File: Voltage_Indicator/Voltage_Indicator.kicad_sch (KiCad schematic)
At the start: 20 parts, among them IC1 TLV2371QDBVRQ1, J1 PET-02-XX-X-VT-LC, U2 IPBT-102-H1-XX-S-RA, U3 PAMC0381D10QDFXRQ1

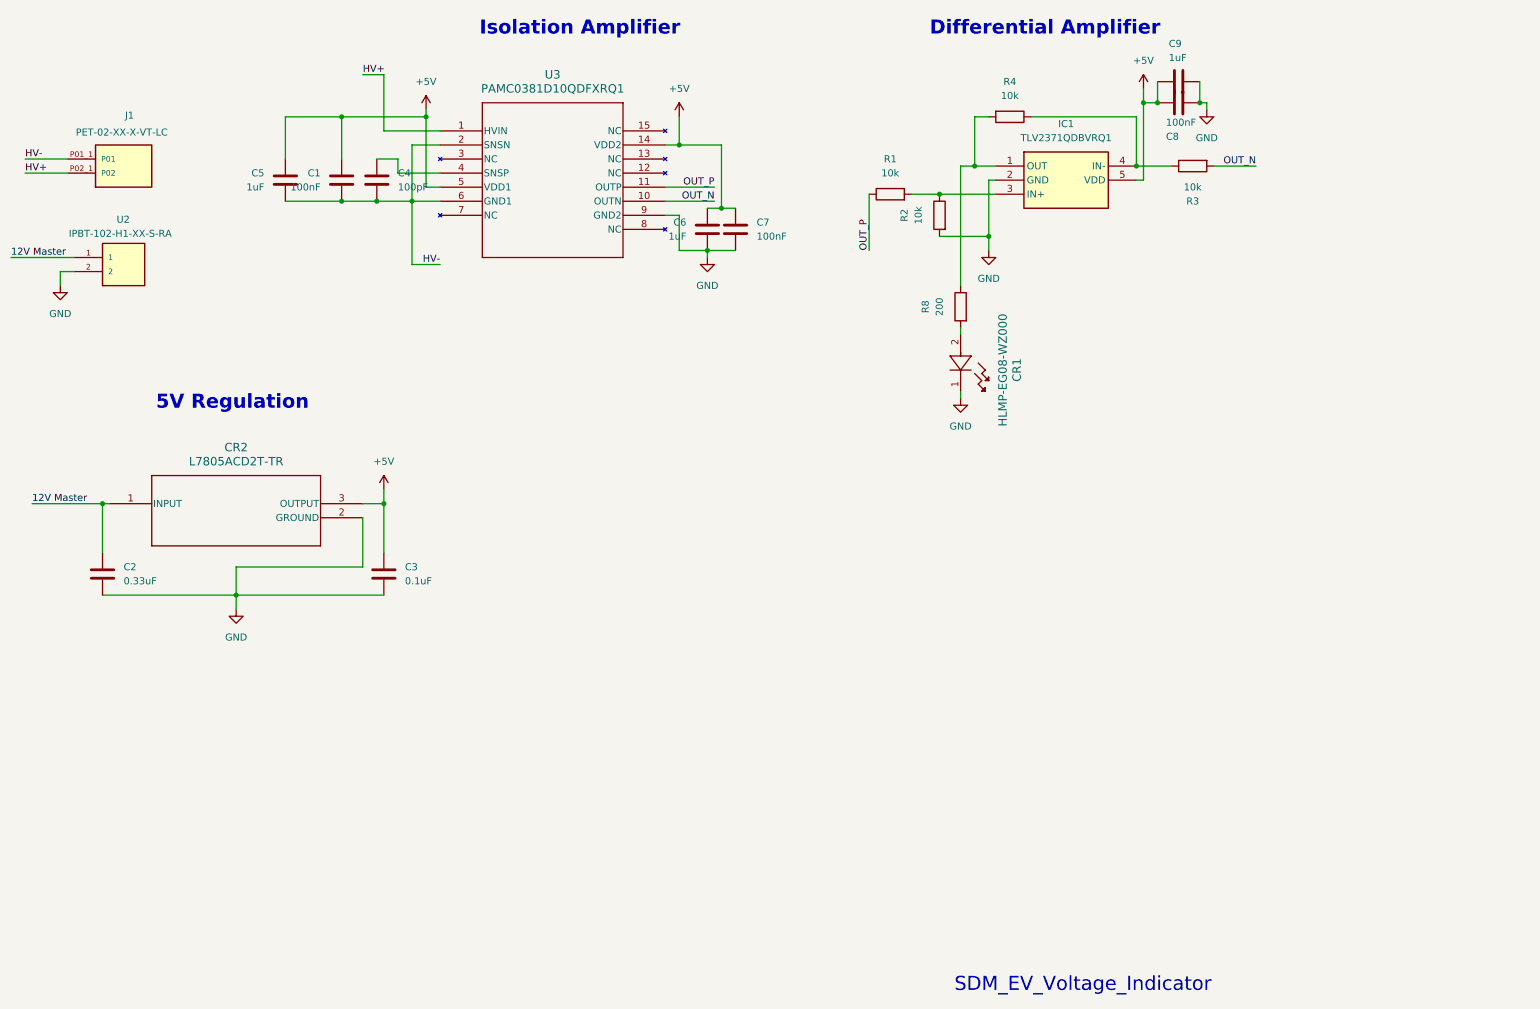
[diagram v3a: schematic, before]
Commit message: Voltage Indicator with comparator :(
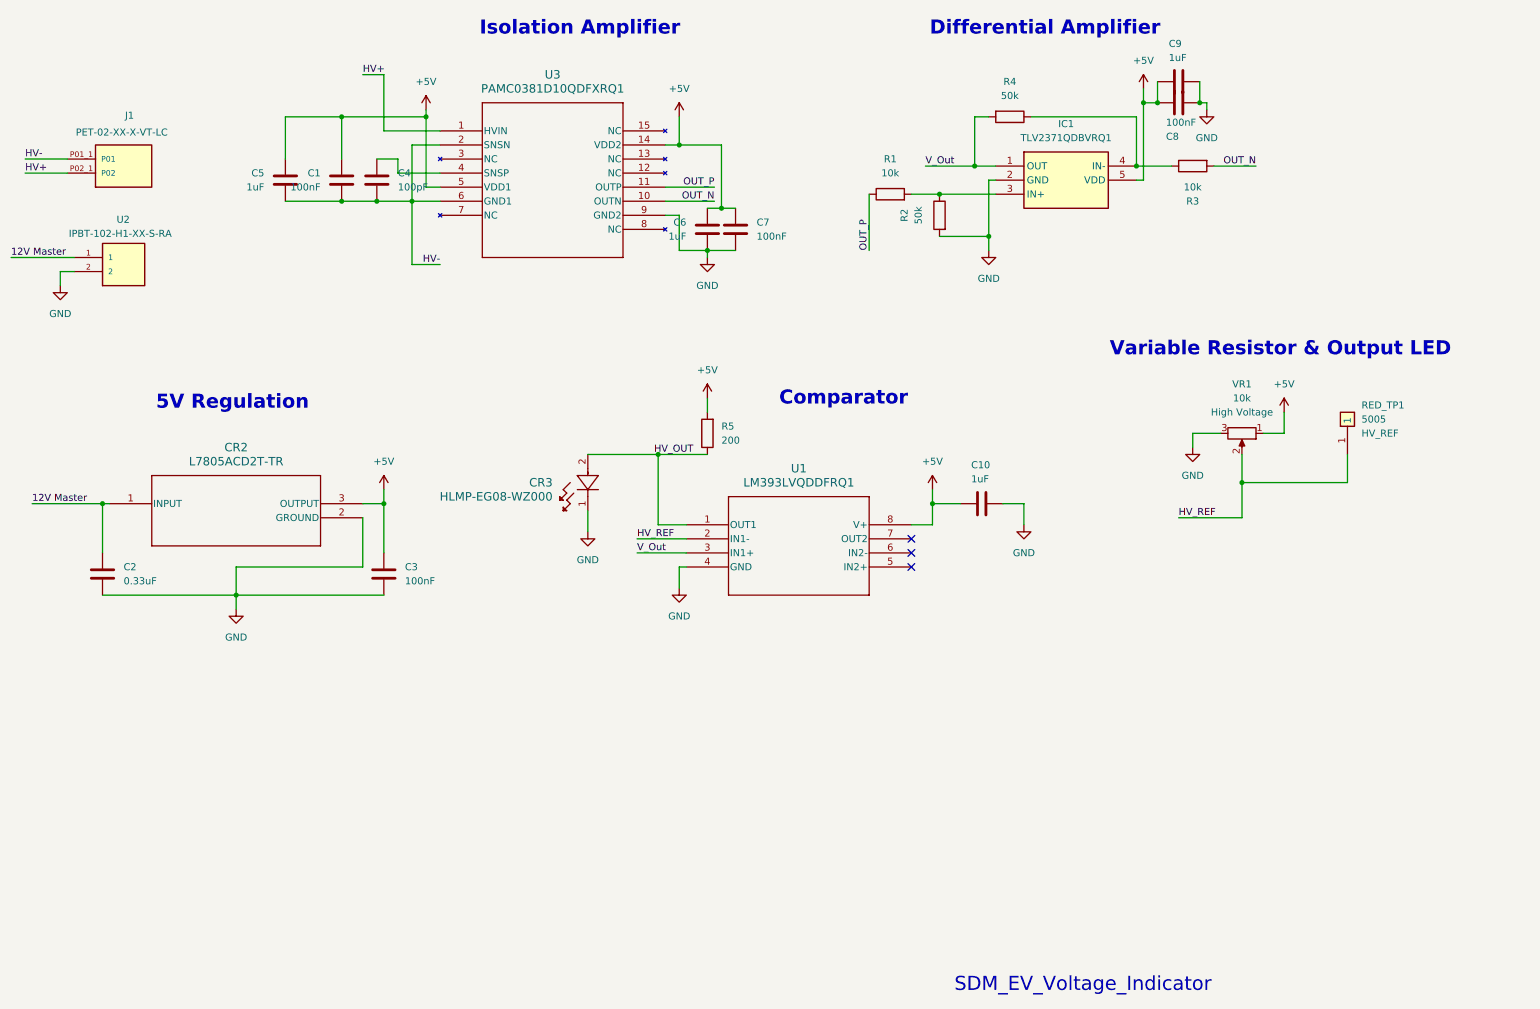
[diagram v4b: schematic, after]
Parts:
- removed CR1: HLMP-EG08-WZ000, Footprints:LED_AVAGO_HLMP_XX08_AVA, symbol Symbols:HLMP-EG08-WZ000
- removed R8: 200, Resistor_SMD:R_0201_0603Metric, symbol Device:R
- added C10: 1uF, Capacitor_SMD:C_0603_1608Metric, symbol Device:C
- added CR3: HLMP-EG08-WZ000, Footprints:LED_AVAGO_HLMP_XX08_AVA, symbol Symbols:HLMP-EG08-WZ000
- added R5: 200, Resistor_SMD:R_0603_1608Metric, symbol Device:R
- added RED_TP1: 5005, SDM_MiscFootprint:5005, symbol SDM_TESTPOINT:5005
- added U1: LM393LVQDDFRQ1, Footprints:SOT-23-THIN8_DDF_TEX, symbol SDM_Parts:LM393LVQDDFRQ1
- added VR1: 10k, SDM_MiscFootprint:3386P1103TLF, symbol SDM_VARIABLE_RESISTOR:3386P-1-103TLF
- C3: value 0.1uF -> 100nF
- R2, R4: value 10k -> 50k
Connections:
- net +5V: now also C10.2, R5.2, U1.8 (V+), VR1.1 (CCW)
- net GND: now also C10.1, CR3.1, U1.4 (GND), VR1.3 (CW)
- net V_Out: now reaches IC1.1 (OUT), R4.2
- net V_Out: now also U1.3 (IN1+)
- new net HV_OUT: CR3.2, R5.1, U1.1 (OUT1)
- new net HV_REF: RED_TP1.1, U1.2 (IN1-), VR1.2 (Wiper)
- no-connect marks 0 -> 3
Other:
- note added: "Comparator"
- note added: "Variable Resistor & Output LED"

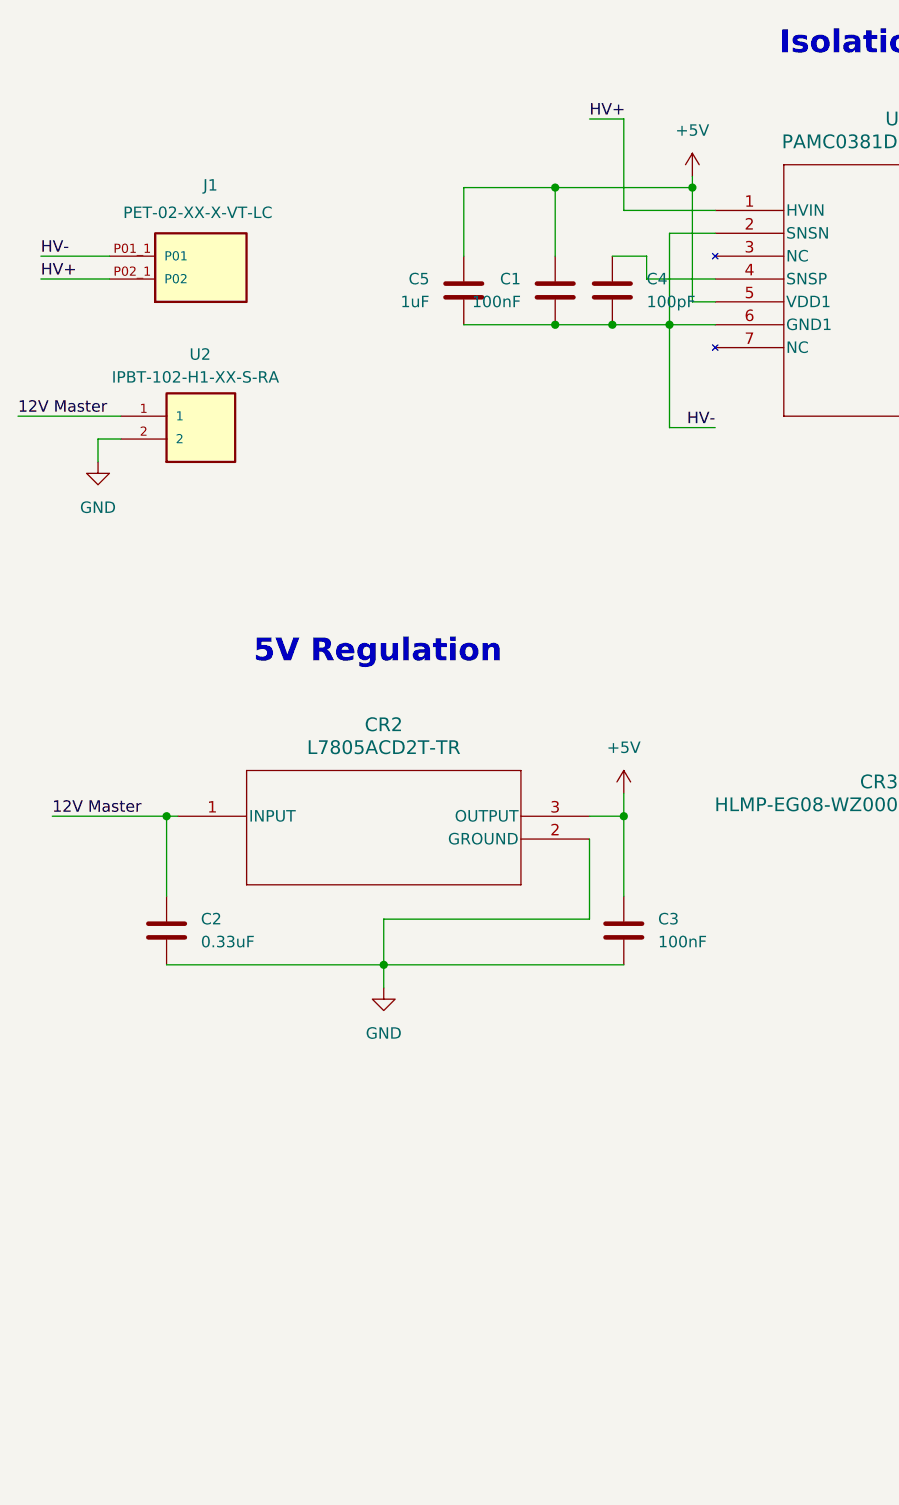
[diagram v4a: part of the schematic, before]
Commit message: Fixed a net in BSPD and added isolated 5V line in voltage indicator
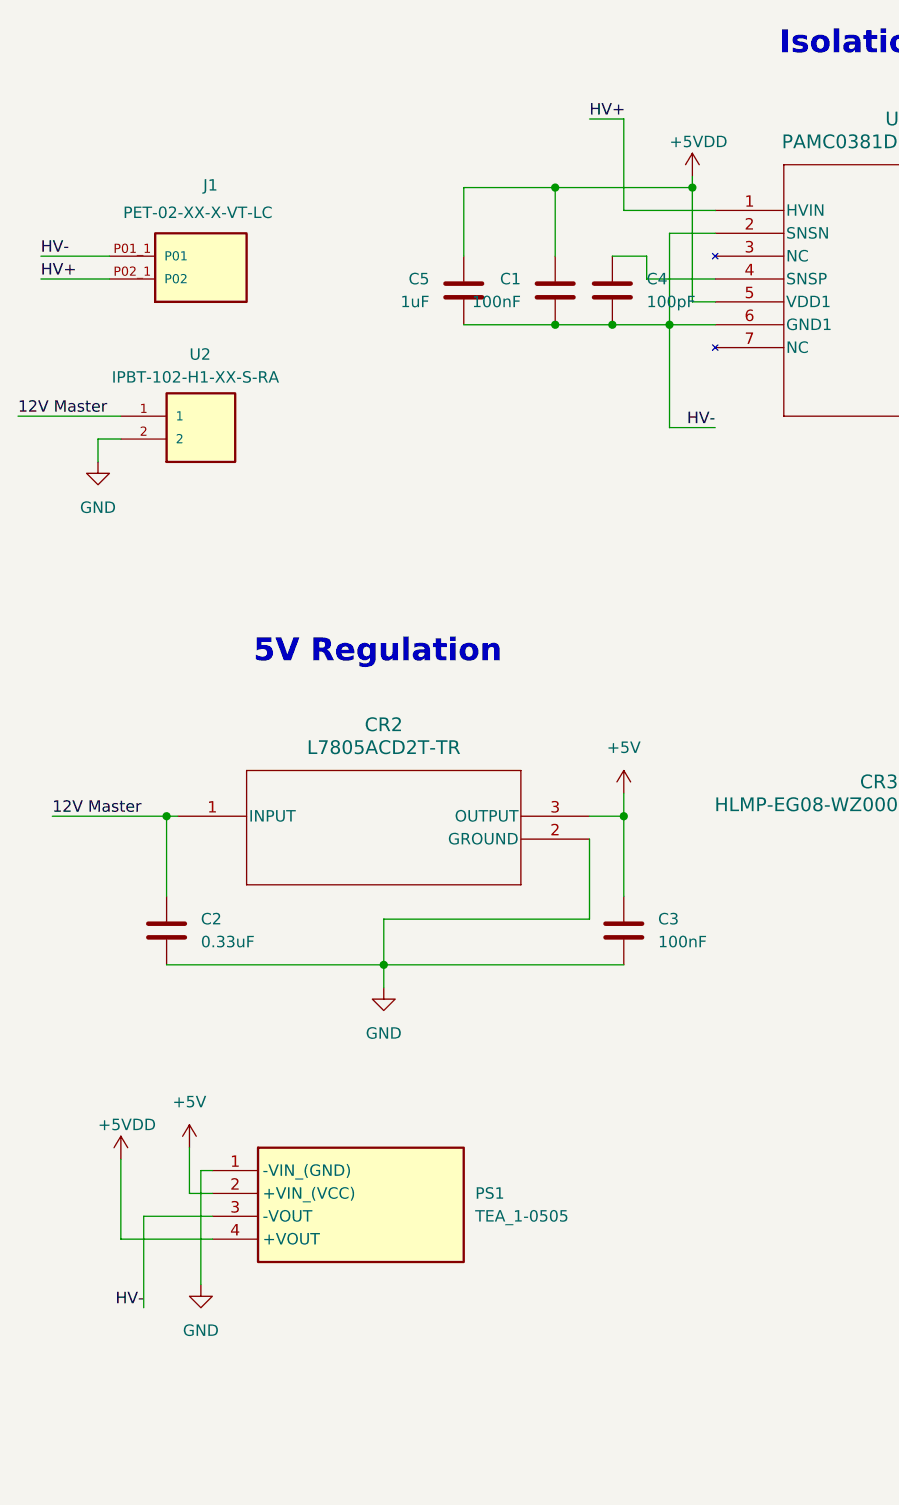
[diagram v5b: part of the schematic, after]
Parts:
- added PS1: TEA_1-0505, Footprints:TEA10505, symbol Symbols:TEA_1-0505
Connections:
- net +5V: now also PS1.2 (+VIN_(VCC)); no longer C1.2, C5.2, U3.5 (VDD1)
- net GND: now also PS1.1 (-VIN_(GND))
- net HV-: now also PS1.3 (-VOUT)
- new net +5VDD: C1.2, C5.2, PS1.4 (+VOUT), U3.5 (VDD1)
